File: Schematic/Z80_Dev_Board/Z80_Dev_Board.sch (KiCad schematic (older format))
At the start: 26 parts, among them U1 74AC08, U2 62256, U3 62256, U4 74AC00, U5 74AC04, U6 Z80 CPU, U7 74HC157, U8 74AC74, X1 4MHz

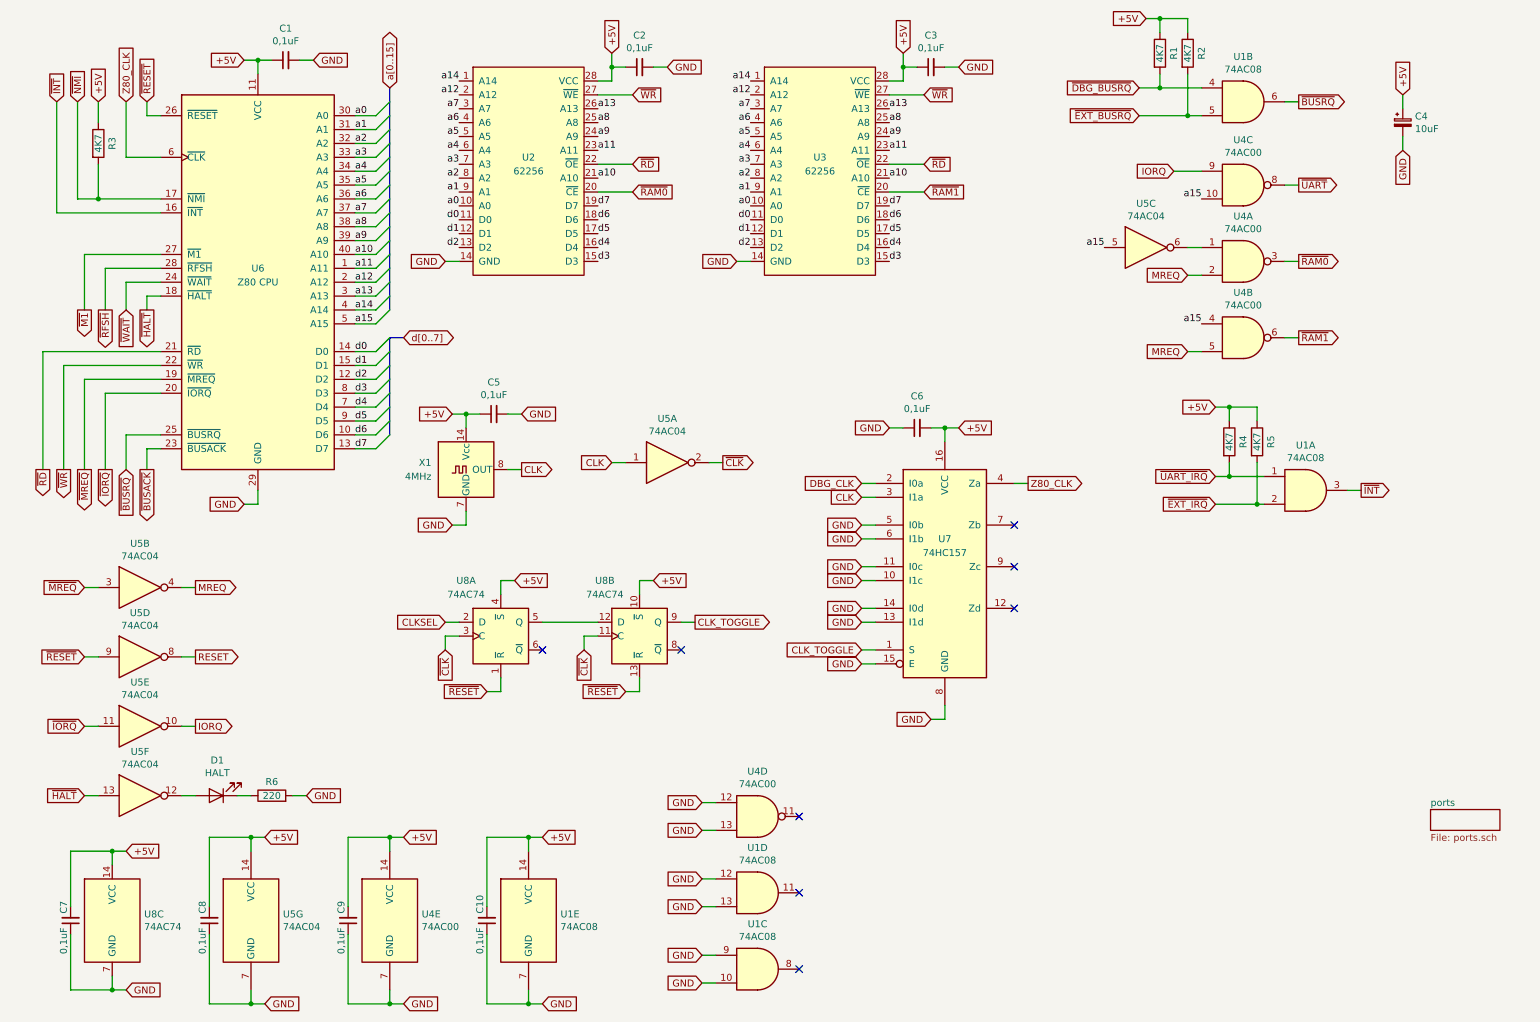
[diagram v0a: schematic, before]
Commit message: Started working on updated PCB with IO decoder
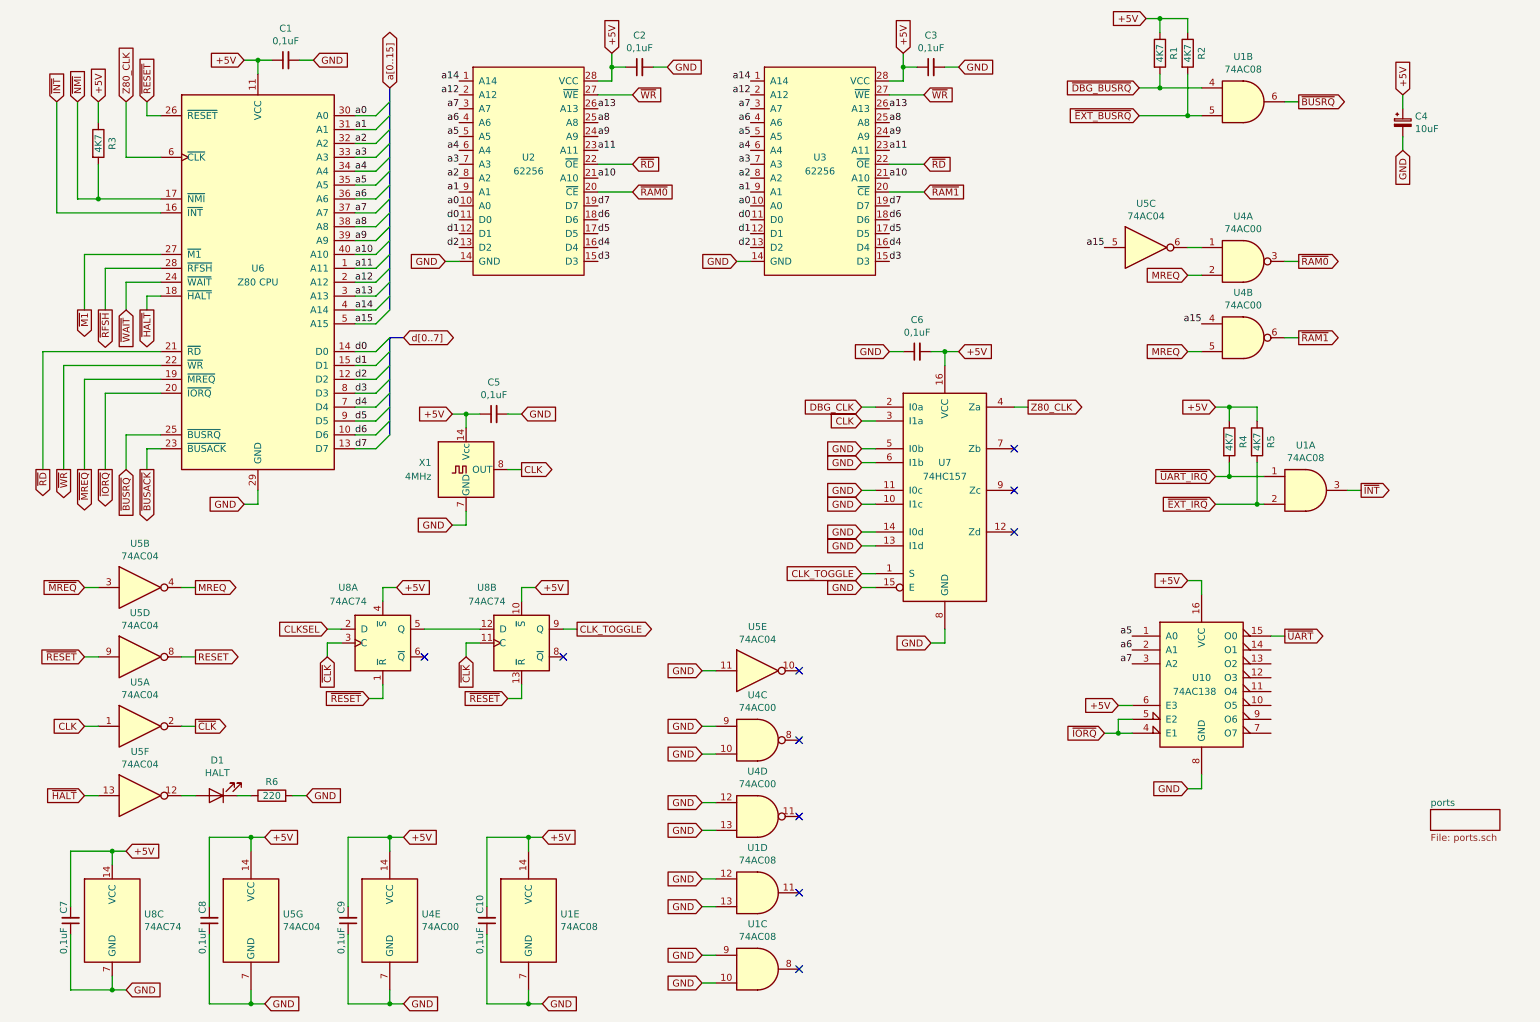
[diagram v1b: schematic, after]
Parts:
- added U10: 74AC138, Package_DIP:DIP-16_W7.62mm_Socket, symbol 74xx:74LS138
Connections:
- net +5V: now also U10.16 (VCC), U10.6 (E3)
- net GND: now also U4.10, U4.9, U5.11, U10.8 (GND)
- net a15: no longer U4.10
- net a5: now also U10.1 (A0)
- net a6: now also U10.2 (A1)
- net a7: now also U10.3 (A2)
- net ~IORQ: now also U10.4 (E1), U10.5 (E2); no longer U5.11
- net ~UART: now also U10.15 (O0); no longer U4.8
- net IORQ: no longer names the net of U5.10
- net IORQ: no longer U4.9
- no-connect marks 8 -> 10
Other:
- moved on the sheet: C6, U4C, U5A, U5E, U7, U8A, U8B

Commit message: New version of the board created
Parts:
- removed R1, R2, R3, R4, R5: 4K7, Resistor_THT:R_Axial_DIN0207_L6.3mm_D2.5mm_P10.16mm_Horizontal, symbol Device:R
- added C10: 0,1uF, Capacitor_SMD:C_1206_3216Metric_Pad1.42x1.75mm_HandSolder, symbol Device:C_Small
- C1: renamed from C7; footprint Capacitor_THT:C_Disc_D5.0mm_W2.5mm_P2.50mm -> Capacitor_SMD:C_1206_3216Metric_Pad1.42x1.75mm_HandSolder
- C2: renamed from C8; footprint Capacitor_THT:C_Disc_D5.0mm_W2.5mm_P2.50mm -> Capacitor_SMD:C_1206_3216Metric_Pad1.42x1.75mm_HandSolder
- C3: renamed from C1; footprint Capacitor_THT:C_Disc_D5.0mm_W2.5mm_P2.50mm -> Capacitor_SMD:C_1206_3216Metric_Pad1.42x1.75mm_HandSolder
- C4: renamed from C9; footprint Capacitor_THT:C_Disc_D5.0mm_W2.5mm_P2.50mm -> Capacitor_SMD:C_1206_3216Metric_Pad1.42x1.75mm_HandSolder
- C5: renamed from C10; footprint Capacitor_THT:C_Disc_D5.0mm_W2.5mm_P2.50mm -> Capacitor_SMD:C_1206_3216Metric_Pad1.42x1.75mm_HandSolder
- C6: renamed from C5; footprint Capacitor_THT:C_Disc_D5.0mm_W2.5mm_P2.50mm -> Capacitor_SMD:C_1206_3216Metric_Pad1.42x1.75mm_HandSolder
- C7: renamed from C2; footprint Capacitor_THT:C_Disc_D5.0mm_W2.5mm_P2.50mm -> Capacitor_SMD:C_1206_3216Metric_Pad1.42x1.75mm_HandSolder
- C8: renamed from C6; footprint Capacitor_THT:C_Disc_D5.0mm_W2.5mm_P2.50mm -> Capacitor_SMD:C_1206_3216Metric_Pad1.42x1.75mm_HandSolder
- C9: renamed from C3; footprint Capacitor_THT:C_Disc_D5.0mm_W2.5mm_P2.50mm -> Capacitor_SMD:C_1206_3216Metric_Pad1.42x1.75mm_HandSolder
- U1: renamed from U8; footprint Package_DIP:DIP-14_W7.62mm_Socket -> Package_SO:SOIC-14_3.9x8.7mm_P1.27mm
- U2: renamed from U5; footprint Package_DIP:DIP-14_W7.62mm_Socket -> Package_SO:SOIC-14_3.9x8.7mm_P1.27mm
- U4: footprint Package_DIP:DIP-14_W7.62mm_Socket -> Package_SO:SOIC-14_3.9x8.7mm_P1.27mm
- U5: renamed from U2; value 62256 -> 71256; footprint Package_DIP:DIP-28_W15.24mm_Socket -> Package_DIP:DIP-28_W7.62mm_Socket
- U6: renamed from U1; footprint Package_DIP:DIP-14_W7.62mm_Socket -> Package_SO:SOIC-14_3.9x8.7mm_P1.27mm
- U7: renamed from U3; value 62256 -> 71256; footprint Package_DIP:DIP-28_W15.24mm_Socket -> Package_DIP:DIP-28_W7.62mm_Socket
- U8: renamed from U7; footprint Package_DIP:DIP-16_W7.62mm_Socket -> Package_SO:SOIC-16_3.9x9.9mm_P1.27mm
- U9: renamed from U10; footprint Package_DIP:DIP-16_W7.62mm_Socket -> Package_SO:SOIC-16_3.9x9.9mm_P1.27mm
- renumbered C4 to C11, R6 to R1, U6 to U3
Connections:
- net +5V: now also C10.1
- net GND: now also C10.2
- net ~IO5: now reaches U9.10 (O5)
- net ~IO4: now reaches U9.11 (O4)
- net ~IO3: now reaches U9.12 (O3)
- net ~IO2: now reaches U9.13 (O2)
- net ~IO1: now reaches U9.14 (O1)
- net ~IO7: now reaches U9.7 (O7)
- net ~IO6: now reaches U9.9 (O6)
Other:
- moved on the sheet: U6A, U6B
